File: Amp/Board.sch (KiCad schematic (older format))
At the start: 22 parts, among them J1 *SDNL/5V, J10 OUTR_1, J12 12V in, J2 IN_1, J3 OUTL_1, J6 THERM, J8 Gain_Conn, U1 SSM3302ACPZ-R7

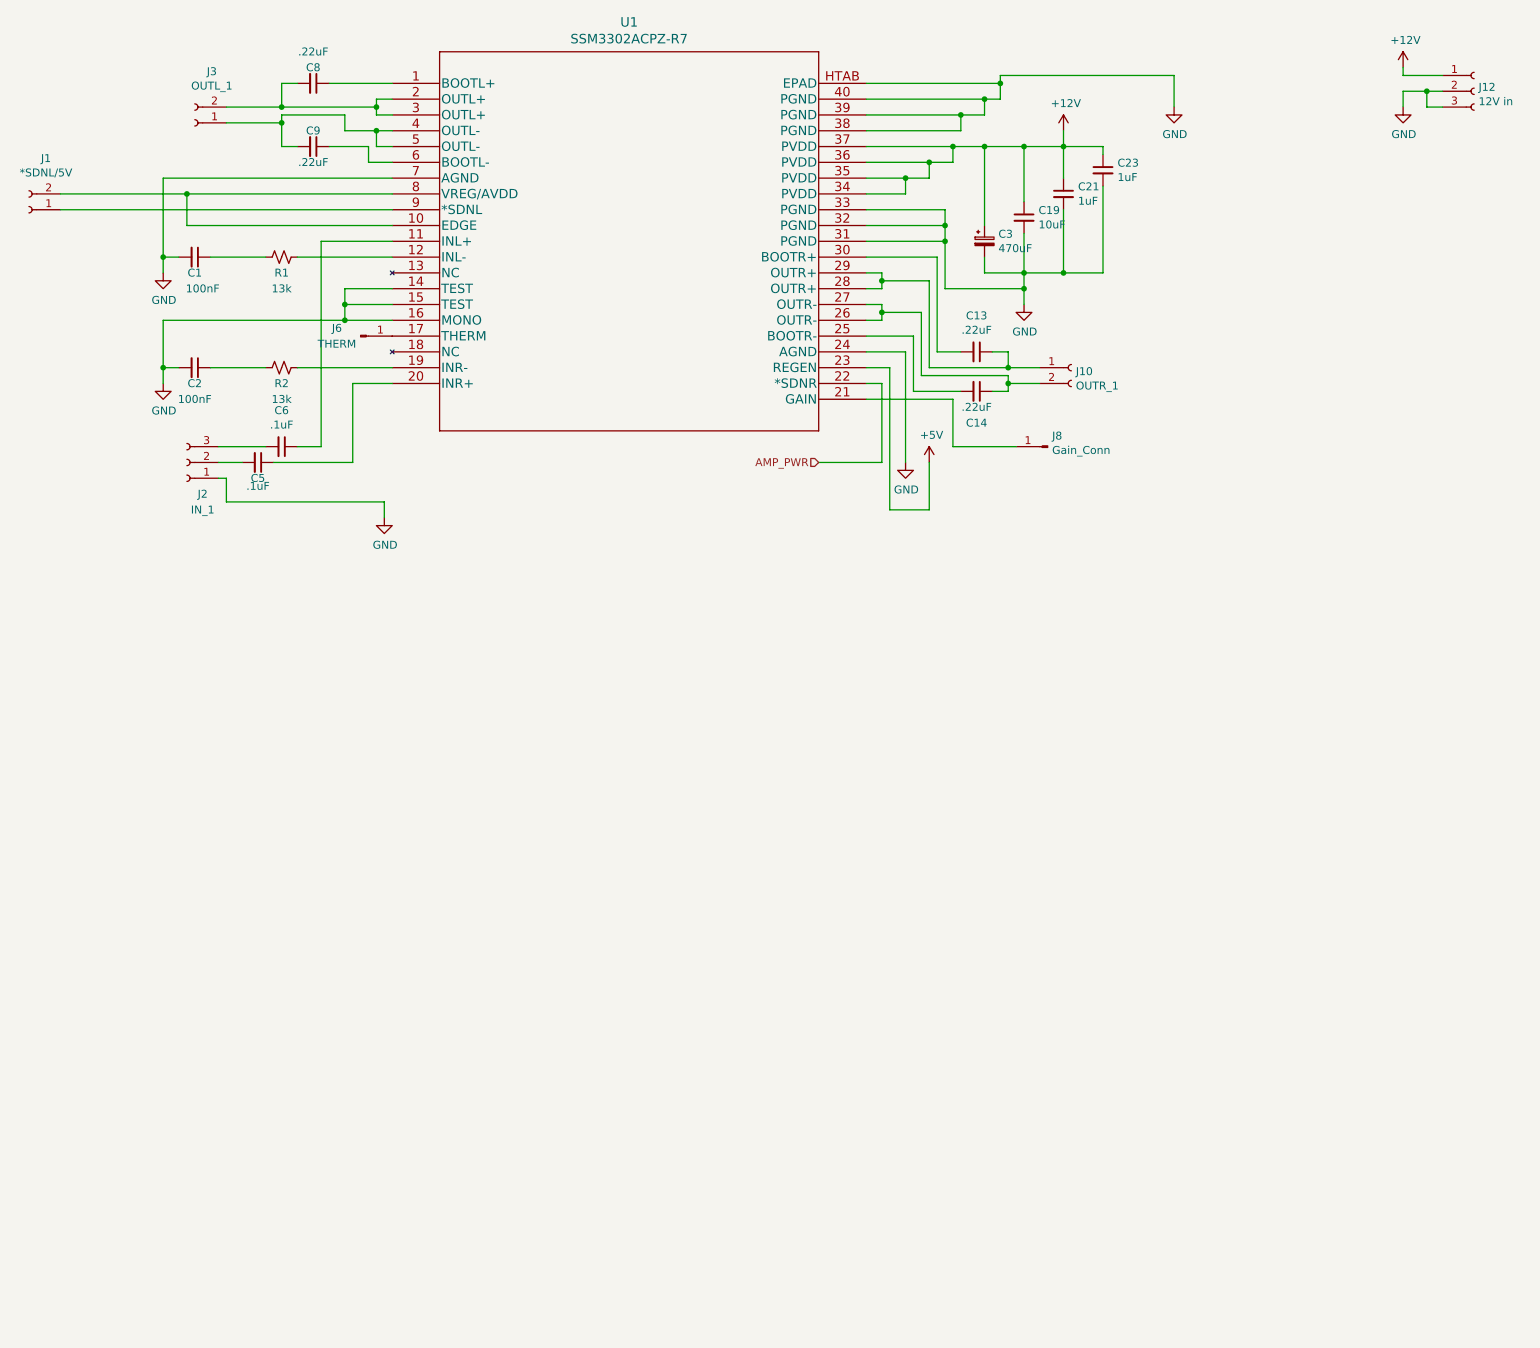
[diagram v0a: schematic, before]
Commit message: finished DSP and AMP
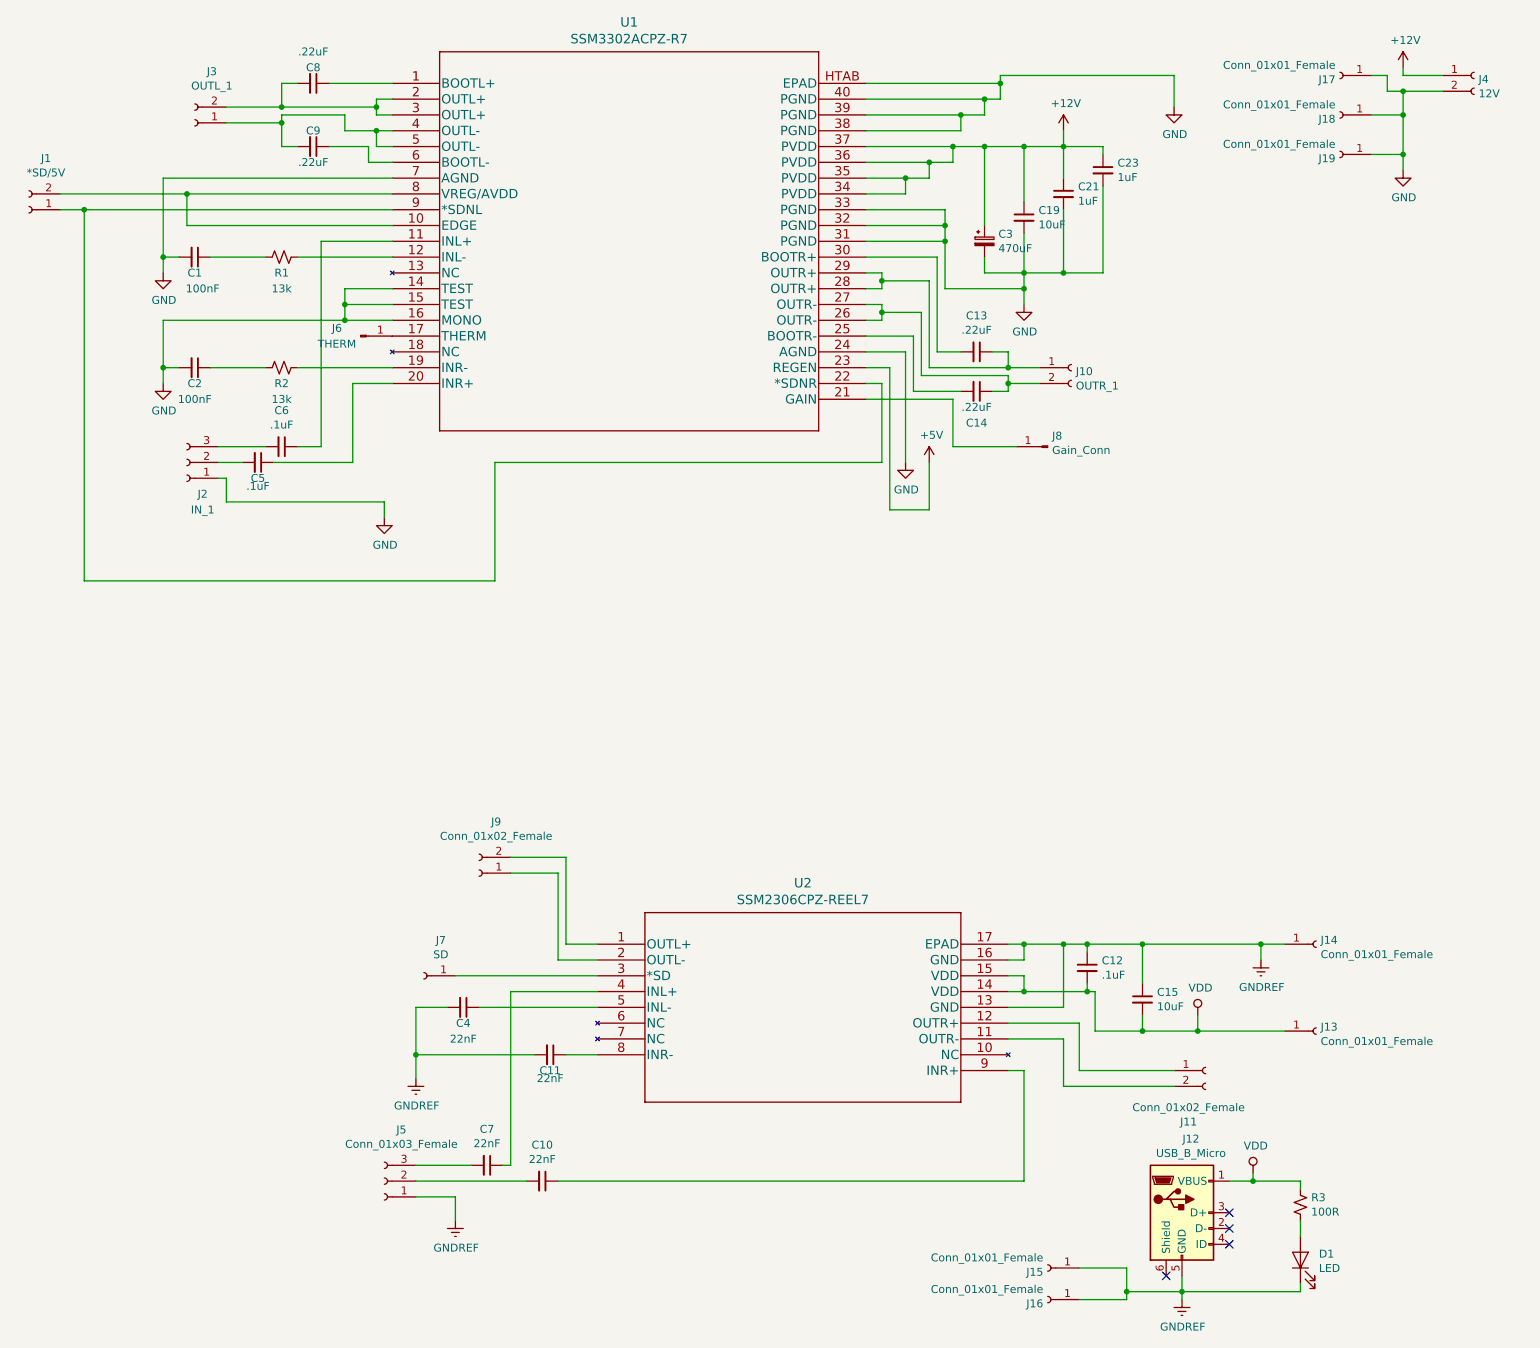
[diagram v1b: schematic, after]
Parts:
- removed J12: 12V in, 691213710003:691213710003, symbol Connector:Conn_01x03_Female
- added C10, C11, C4, C7: 22nF, Capacitor_SMD:C_0805_2012Metric_Pad1.15x1.40mm_HandSolder, symbol Device:C_Small
- added C12: .1uF, Capacitor_SMD:C_0805_2012Metric_Pad1.15x1.40mm_HandSolder, symbol Device:C_Small
- added C15: 10uF, Capacitor_SMD:C_0805_2012Metric_Pad1.15x1.40mm_HandSolder, symbol Device:C_Small
- added D1: LED, LED_SMD:LED_0805_2012Metric_Pad1.15x1.40mm_HandSolder, symbol Device:LED
- added J11, J9: Conn_01x02_Female, WJ250A-3.50-2P:WJ250A3502P, symbol Connector:Conn_01x02_Female
- added J12: USB_B_Micro, MicroUSB:C77238, symbol Connector:USB_B_Micro
- added J13, J14: Conn_01x01_Female, Connector_PinHeader_2.54mm:PinHeader_1x01_P2.54mm_Vertical, symbol Connector:Conn_01x01_Female
- added J15, J16, J17, J18, J19: Conn_01x01_Female, MountingHole:MountingHole_3.2mm_M3_ISO7380_Pad, symbol Connector:Conn_01x01_Female
- added J4: 12V, WJ250A-3.50-2P:WJ250A3502P, symbol Connector:Conn_01x02_Female
- added J5: Conn_01x03_Female, 691213710003:691213710003, symbol Connector:Conn_01x03_Female
- added J7: SD, Connector_PinHeader_2.54mm:PinHeader_1x01_P2.54mm_Vertical, symbol Connector:Conn_01x01_Female
- added R3: 100R, Resistor_SMD:R_0805_2012Metric_Pad1.15x1.40mm_HandSolder, symbol Device:R_Small_US
- added U2: SSM2306CPZ-REEL7, SSM2306:SSM2306CPZ-REEL7, symbol SSM2306:SSM2306CPZ-REEL7
- J1: value *SDNL/5V -> *SD/5V; footprint WJ250A-3.50-2P:WJ250A3502P -> Connector_PinHeader_2.54mm:PinHeader_1x02_P2.54mm_Vertical
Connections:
- net AMP_PWR is gone; now on an unnamed net: U1.22 (*SDNR)
- net +12V: now also J4.1 (Pin_1)
- net GND: now also J17.1 (Pin_1), J18.1 (Pin_1), J19.1 (Pin_1), J4.2 (Pin_2)
- new net: J9.2 (Pin_2), U2.1 (OUTL+)
- new net: J11.2 (Pin_2), U2.11 (OUTR-)
- new net: J11.1 (Pin_1), U2.12 (OUTR+)
- new net: J9.1 (Pin_1), U2.2 (OUTL-)
- new net: J7.1 (Pin_1), U2.3 (*SD)
- new net: C7.1, U2.4 (INL+)
- new net: C4.1, U2.5 (INL-)
- new net: C11.1, U2.8 (INR-)
- new net: C10.1, U2.9 (INR+)
- new net: C10.2, J5.2 (Pin_2)
- new net: C7.2, J5.3 (Pin_3)
- new net: D1.2 (A), R3.2
- new net GNDREF: C11.2, C12.1, C15.1, C4.2, D1.1 (K), J12.5 (GND), J14.1 (Pin_1), J15.1 (Pin_1), J16.1 (Pin_1), J5.1 (Pin_1), U2.13 (GND), U2.16 (GND), U2.17 (EPAD)
- new net VDD: C12.2, C15.2, J12.1 (VBUS), J13.1 (Pin_1), R3.1, U2.14 (VDD), U2.15 (VDD)
- no-connect marks 0 -> 4
